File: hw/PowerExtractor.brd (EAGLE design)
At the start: 100 x 80 mm, 92 parts, among them IC1 LM358D, Q1 BSS84, Q3 BC847SMD, Q4 BC847SMD, Q5 BC847SMD, Q6 BC847SMD, T1 IRL530N, T2 IRF7416, T3 IRLL014N_, T4 IRLL014N_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

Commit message: Routing of board
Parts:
- moved JP9 59.3 mm to (50.8, 47.0)
- moved C7 51.0 mm to (59.7, 24.1)
- moved R5 50.6 mm to (59.7, 30.5)
- moved R18 35.0 mm to (57.1, 53.3), flipped to the bottom, turned to 0 degrees
- moved R4 34.3 mm to (57.1, 21.6), turned to 180 degrees
- moved R20 23.4 mm to (68.6, 31.8)
- moved OPH1 15.3 mm to (85.1, 63.5)
- moved D8 8.52 mm to (58.4, 62.2), turned to 180 degrees
- moved R7 7.73 mm to (48.3, 53.3), turned to 270 degrees
- moved D7 7.18 mm to (50.8, 55.9), turned to 270 degrees
- moved C8 5.08 mm to (50.8, 49.5)
- moved R9 4.02 mm to (55.9, 3.81), turned to 90 degrees
- moved R10 3.81 mm to (55.9, 11.4)
- moved Q4 3.59 mm to (55.9, 57.1)
- moved R17 3.59 mm to (59.7, 55.9)
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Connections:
- removed net N$21: HEAD_LED.1, U$1.VO+
- removed net N$22: HEAD_LED.2, U$1.VO-
- new net N$13: HEAD_LED.2, U$1.VO+
- new net N$15: HEAD_LED.1, U$1.VO-
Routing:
- net BAT+FUSED: track 23.3 -> 105.5 mm
- net GND: track 189.4 -> 266.8 mm
- net N$24: track 0.00 -> 57.8 mm
- net +5V: track 30.7 -> 73.0 mm
- net N$35: track 0.00 -> 41.4 mm
- net N$34: track 0.00 -> 40.4 mm
- net ARDUINO_VIN: track 0.00 -> 35.2 mm
- net N$19: track 0.00 -> 34.2 mm
- net ARDUINO_VOUT_SENSE: track 0.00 -> 31.5 mm
- net N$14: track 0.00 -> 23.8 mm
- net ARDUINO_LIGHT_IN: track 4.99 -> 26.7 mm
- net N$13: track 0.00 -> 15.5 mm
- net VIN: track 44.8 -> 53.4 mm
- net N$20: track 0.00 -> 8.51 mm
- net N$9: track 1.87 -> 9.69 mm
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
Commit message: Routing
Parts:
- IC1: value LM358D -> LM358N; device linear:SO08 -> linear:DIL08
- moved R12 10.2 mm to (74.9, 49.5), flipped to the top, turned to 180 degrees
- moved IC1 5.08 mm to (25.4, 57.1)
- moved R22 1.80 mm to (22.9, 55.9), flipped to the bottom, turned to 180 degrees
- moved R23 1.27 mm to (22.9, 58.4), flipped to the bottom, turned to 180 degrees
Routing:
- net N$24: track 57.8 -> 0.00 mm
- net ARDUINO_CHARGE_SENSE: track 1.27 -> 44.8 mm
- net +5V: track 73.0 -> 34.4 mm
- net GND: track 266.8 -> 300.9 mm
- net ARDUINO_ROTATION_INT: track 2.60 -> 25.8 mm
- net N$5: track 8.50 -> 0.00 mm
- net N$8: track 6.57 -> 2.84 mm
- net ARDUINO_LIGHT_IN: track 26.7 -> 29.4 mm
- net N$27: track 2.40 -> 0.00 mm
- net N$11: track 1.27 -> 2.54 mm

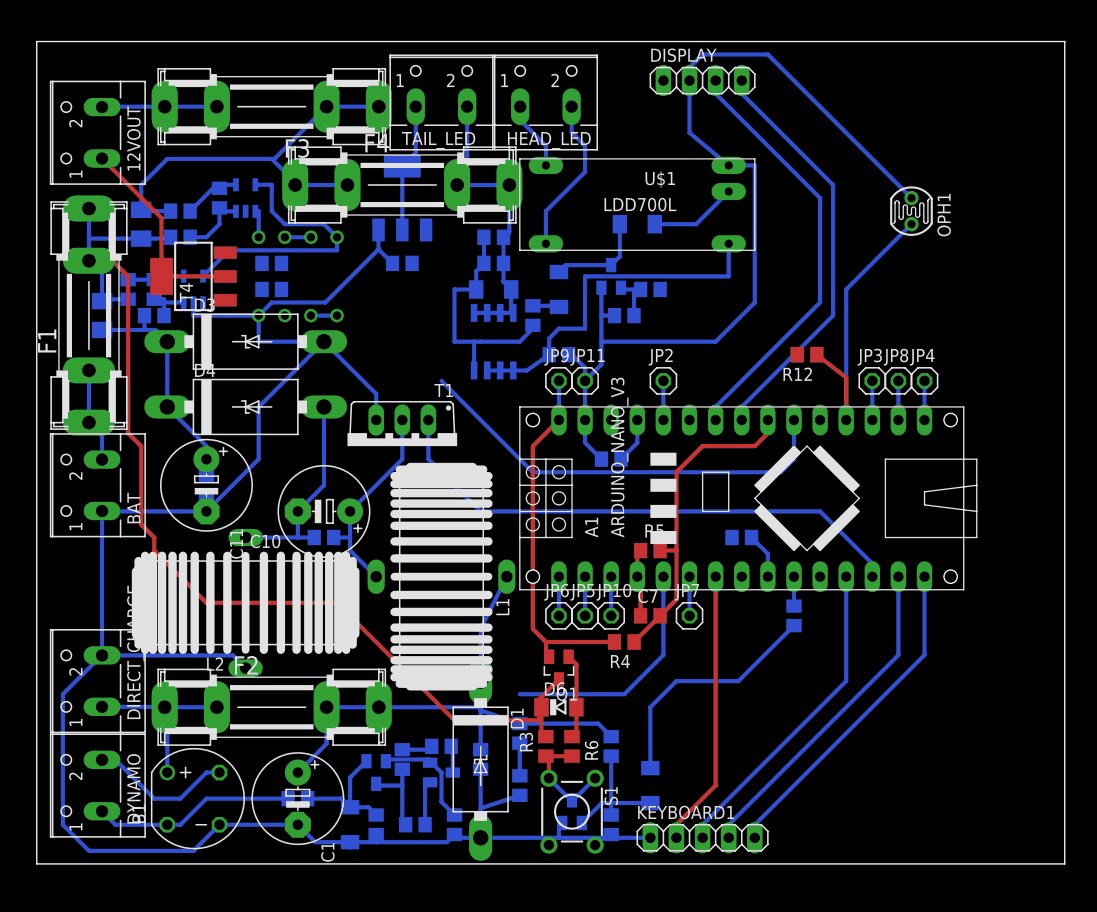
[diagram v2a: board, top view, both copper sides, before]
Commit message: Refactored layout
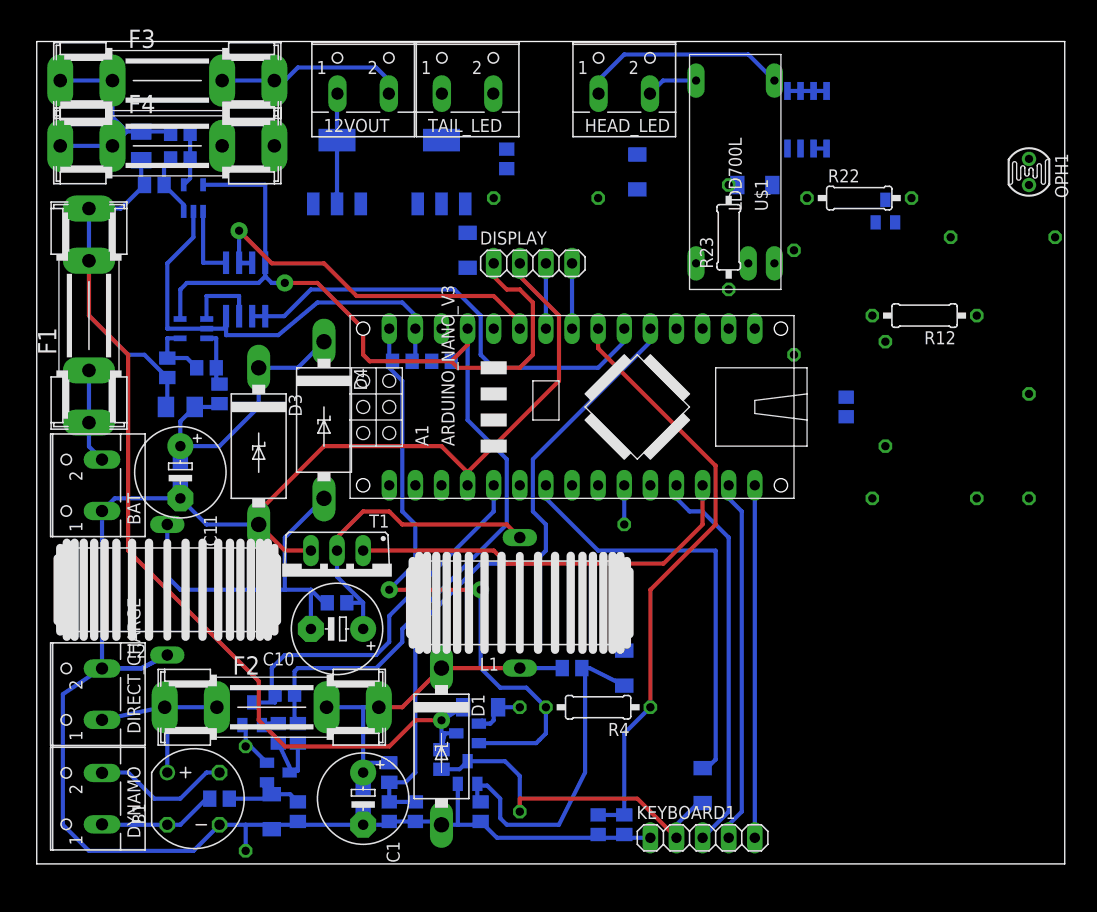
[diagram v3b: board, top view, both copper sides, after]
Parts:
- removed JP10, JP11, JP2, JP3, JP4, JP5, JP6, JP7, JP8, JP9: (no value), pinhead:1X01
- removed S1: (no value), triakcz:TL1105
- added C12: 10n, rcl:C0805
- added C14: 1uF/50V, rcl:C0805
- added D10: 1N4148MINIMELF, triakcz:SOD80C
- IC1: value LM358N -> LM358D; device linear:DIL08 -> linear:SO08
- R1, R10, R15, R16, R24, R25, R29, R3, R30, R31, R5, R9: device rcl:R0805 -> rcl:M0805
- R11, R12, R17, R18, R19, R20, R21, R22, R23, R26, R4, R6, R7: device rcl:R0805 -> rcl:0207/10
- moved R22 57.8 mm to (80.0, 64.8), flipped to the top, turned to 0 degrees
- moved R21 55.7 mm to (86.4, 35.6)
- moved R7 49.9 mm to (96.5, 40.6)
- moved R23 44.5 mm to (67.3, 61.0), flipped to the top, turned to 90 degrees
- moved R18 37.6 mm to (94.0, 61.0)
- moved T2 37.4 mm to (74.9, 72.4)
- moved C8 28.4 mm to (78.7, 44.5), turned to 270 degrees
- moved Q4 27.4 mm to (82.5, 63.5)
- moved 12VOUT 27.1 mm to (31.8, 76.2), turned to 0 degrees
- moved R5 26.8 mm to (57.1, 3.81), flipped to the bottom, turned to 90 degrees
- moved DISPLAY 24.3 mm to (48.3, 58.4)
- moved F4 23.2 mm to (12.7, 69.8)
- moved C7 20.9 mm to (54.6, 3.81), flipped to the bottom, turned to 90 degrees
- moved R26 20.5 mm to (20.3, 6.35)
- moved R20 19.8 mm to (82.5, 45.7), turned to 270 degrees
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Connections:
- removed net N$33: A1.D4, KEYBOARD1.2
- removed net N$38: A1.D1/TX, JP6.1
- removed net N$39: A1.D0/RX, JP5.1
- removed net N$40: A1.D3, JP7.1
- removed net N$42: A1.A7, JP2.1
- removed net N$43: A1.REF, JP3.1
- removed net N$44: A1.RST.1, A1.RST.2, JP10.1
- removed net N$45: A1.D13, JP4.1
- new net N$22: A1.D4, D10.C
- net +3V3: no longer JP8.1
- net ARDUINO_VIN: now also C14.1; no longer JP9.1
- net ARDUINO_VIN_ANALOG: now also C12.2
- net GND: now also C12.1, C14.2; no longer JP11.1, S1.1, S1.2
- net N$6: now also D10.A, KEYBOARD1.2; no longer S1.3, S1.4
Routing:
- net +5V: track 34.4 -> 130.6 mm, vias 0 -> 1
- net ARDUINO_VIN_ANALOG: track 3.18 -> 64.1 mm
- net GND: track 300.9 -> 240.1 mm
- net N$22: track 0.00 -> 41.8 mm
- net N$35: track 41.4 -> 6.35 mm
- net N$11: track 2.54 -> 37.4 mm, vias 0 -> 1
- net N$34: track 40.4 -> 6.35 mm
- net N$19: track 34.2 -> 1.27 mm
- net ARDUINO_LIGHT_IN: track 29.4 -> 0.00 mm
- net N$33: track 27.0 -> 0.00 mm
- net ARDUINO_VOUT_SENSE: track 31.5 -> 58.3 mm
- net ARDUINO_VIN: track 35.2 -> 61.8 mm, vias 0 -> 2
- net LIGHTVCC: track 30.0 -> 3.81 mm
- net N$6: track 11.1 -> 35.3 mm
- net N$14: track 23.8 -> 0.00 mm
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
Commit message: Completely routed
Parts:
- removed OPH1: VT90N1, photo-elements:VT900
- removed T3, T4: IRLL014N_, triakcz:SOT223
- added PHOTORESIST: (no value), pinhead:1X02
- added Q2: IRL530, transistor-power:TO220BV
- added Q7: IRF530, transistor-power:TO220BV
- R18, R19, R21, R7: device rcl:0207/10 -> rcl:M0805
- R23: device rcl:0207/10 -> rcl:R0805
- moved R21 63.1 mm to (30.5, 64.8), flipped to the top, turned to 90 degrees
- moved R7 52.2 mm to (52.1, 67.9), turned to 0 degrees
- moved R23 44.5 mm to (22.9, 63.5)
- moved R20 37.5 mm to (48.3, 61.0), turned to 180 degrees
- moved C8 33.7 mm to (55.2, 68.6), flipped to the top, turned to 90 degrees
- moved R12 33.1 mm to (53.3, 55.9)
- moved R22 32.4 mm to (48.3, 58.4)
- moved T2 32.0 mm to (43.2, 68.6), turned to 270 degrees
- moved R18 24.8 mm to (69.2, 59.7), turned to 270 degrees
- moved D7 16.5 mm to (57.1, 66.0), turned to 0 degrees
- moved Q4 15.2 mm to (67.3, 63.5)
- moved R17 14.4 mm to (63.5, 44.5), turned to 0 degrees
- moved D10 8.25 mm to (61.6, 15.2)
- moved R19 7.41 mm to (53.3, 71.1), turned to 90 degrees
- moved D8 6.54 mm to (64.1, 62.9), turned to 270 degrees
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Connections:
- net ARDUINO_LIGHT_IN: now also PHOTORESIST.2; no longer OPH1.1
- net GND: now also PHOTORESIST.1, Q2.S, Q7.S; no longer OPH1.2, T3.3, T4.3
- net N$24: now also Q2.G; no longer T3.1
- net N$25: now also Q2.D; no longer T3.2, T3.4
- net N$27: now also Q7.G; no longer T4.1
- net N$28: now also Q7.D; no longer T4.2, T4.4
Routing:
- net GND: track 240.1 -> 371.2 mm
- net LIGHTVCC: track 3.81 -> 55.9 mm
- net N$19: track 1.27 -> 46.3 mm, vias 0 -> 1
- net ARDUINO_LIGHT_IN: track 0.00 -> 41.3 mm
- net ARDUINO_OUT_TAIL_LIGHT: track 0.00 -> 31.5 mm
- net ARDUINO_OUT_CHARGE_OUTPUT_CONTROL: track 0.00 -> 24.2 mm
- net N$17: track 0.00 -> 22.0 mm
- net N$27: track 0.00 -> 22.0 mm
- net N$22: track 41.8 -> 24.9 mm
- net N$14: track 0.00 -> 14.9 mm
- net N$24: track 0.00 -> 14.8 mm
- net N$25: track 0.00 -> 14.2 mm
- net ARDUINO_MAIN_LIGHT_CTRL: track 0.00 -> 10.3 mm
- net N$9: track 0.00 -> 9.09 mm
- net N$26: track 38.2 -> 31.5 mm
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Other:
- board size 100 x 80 mm -> 74.6 x 80 mm

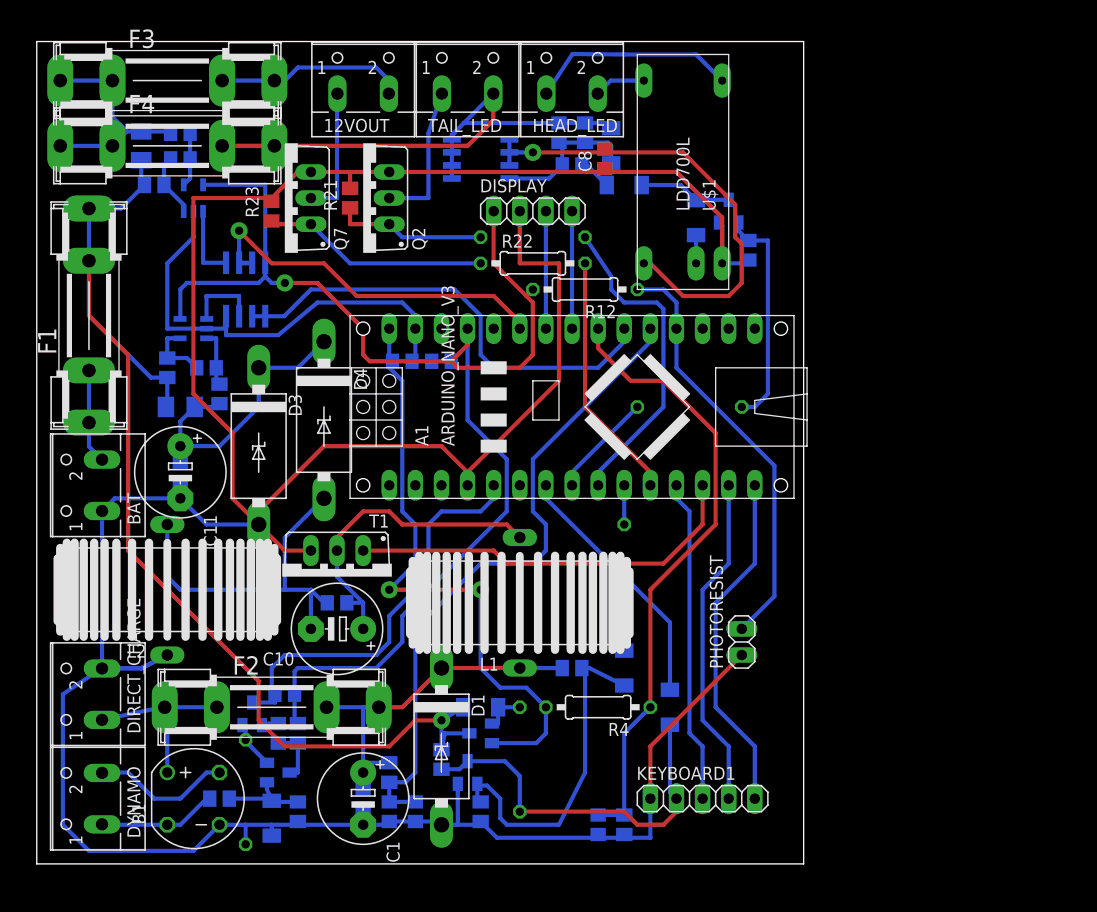
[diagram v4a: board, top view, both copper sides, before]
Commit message: set reasonable width of power lines
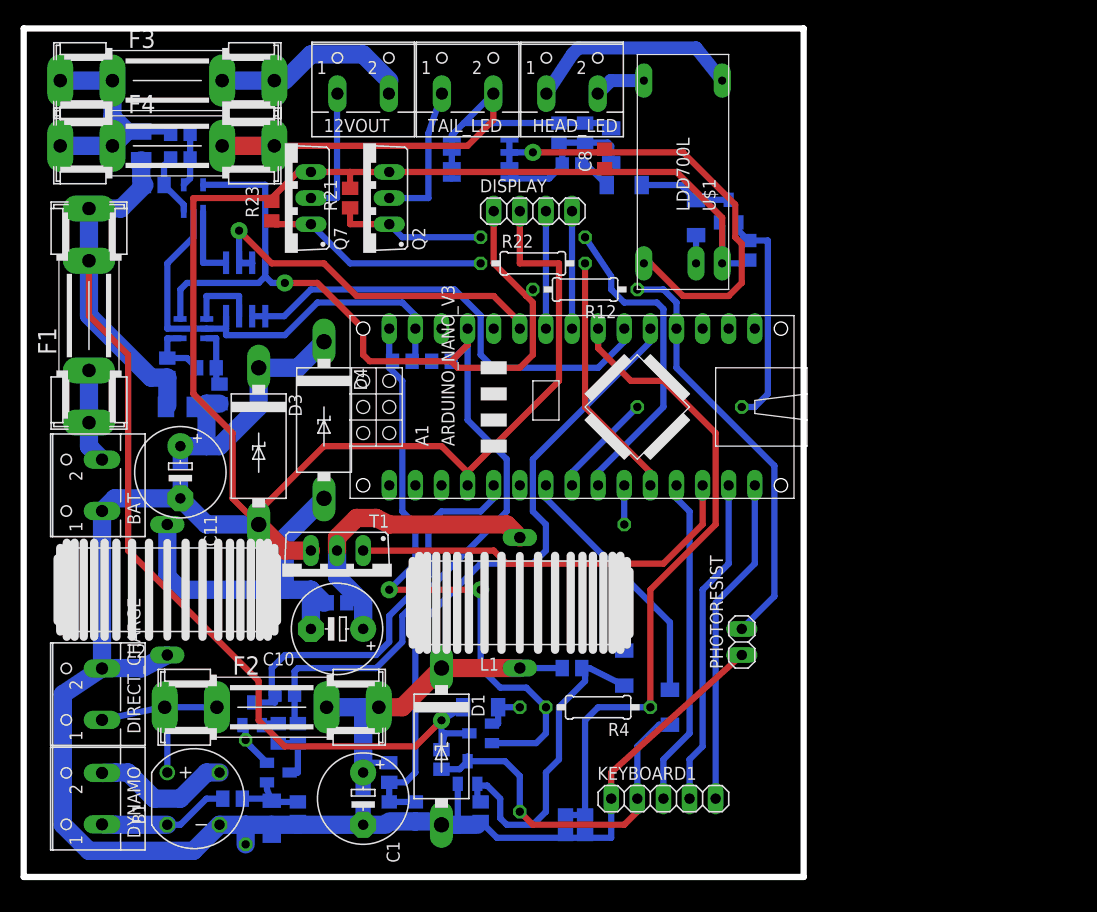
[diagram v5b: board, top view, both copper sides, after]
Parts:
- moved KEYBOARD1 3.81 mm to (61.0, 6.35)
- moved R5 3.81 mm to (53.3, 3.81)
- moved C7 3.17 mm to (51.4, 3.81)
- moved R24 1.27 mm to (19.1, 6.35)
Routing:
- net ARDUINO_VOUT_SENSE: track 60.1 -> 64.0 mm
- net N$6: track 37.5 -> 35.4 mm
- net N$36: track 33.6 -> 32.1 mm
- net GND: track 371.2 -> 369.9 mm
- net HUB_1: track 11.5 -> 12.8 mm
- net N$29: track 8.65 -> 7.38 mm
- net +OUT: track 18.6 -> 19.6 mm
- net N$4: track 33.0 -> 31.9 mm
- net OUTPUT_TO_SENSE: track 28.9 -> 29.9 mm
- net N$15: track 20.2 -> 20.9 mm
- net N$2: track 31.4 -> 30.8 mm
- net N$37: track 32.6 -> 32.1 mm
- net N$26: track 31.5 -> 32.1 mm
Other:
- board size 74.6 x 80 mm -> 75.9 x 82.5 mm

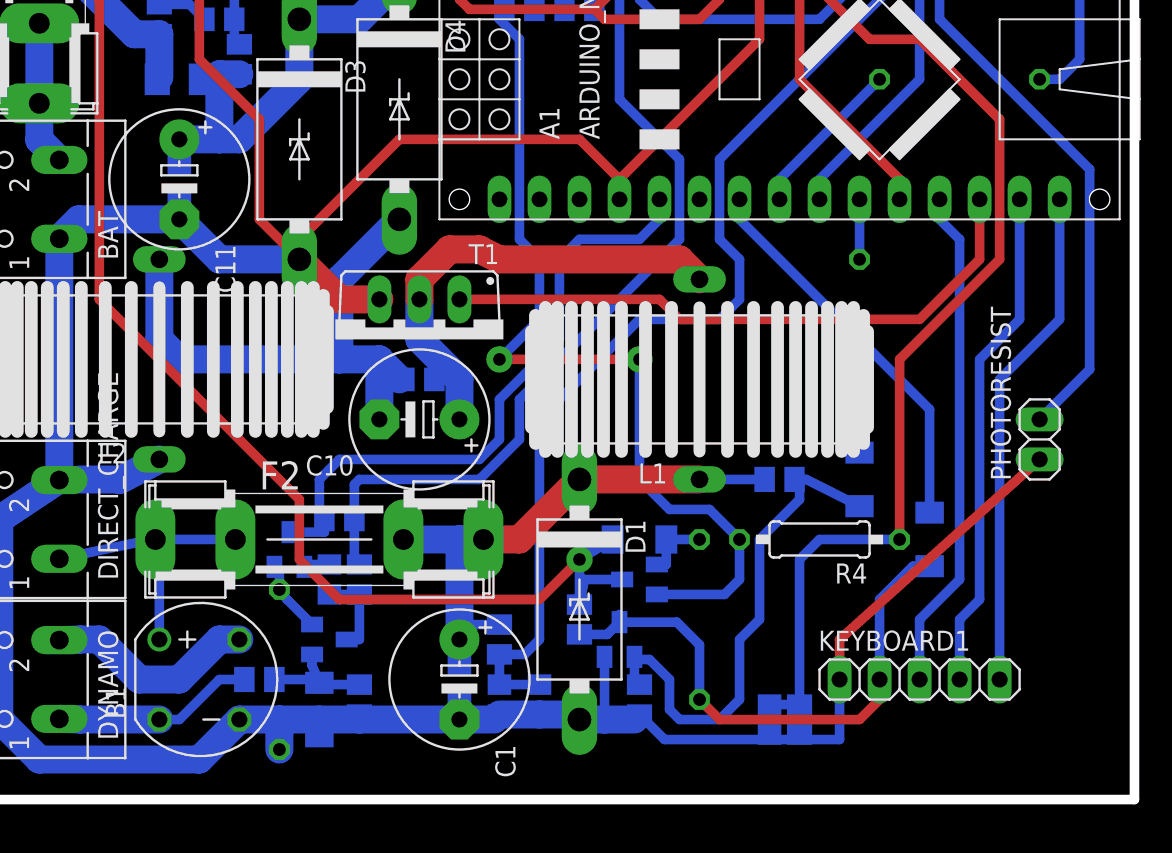
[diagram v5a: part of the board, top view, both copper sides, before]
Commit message: Fixed speed sense circuit
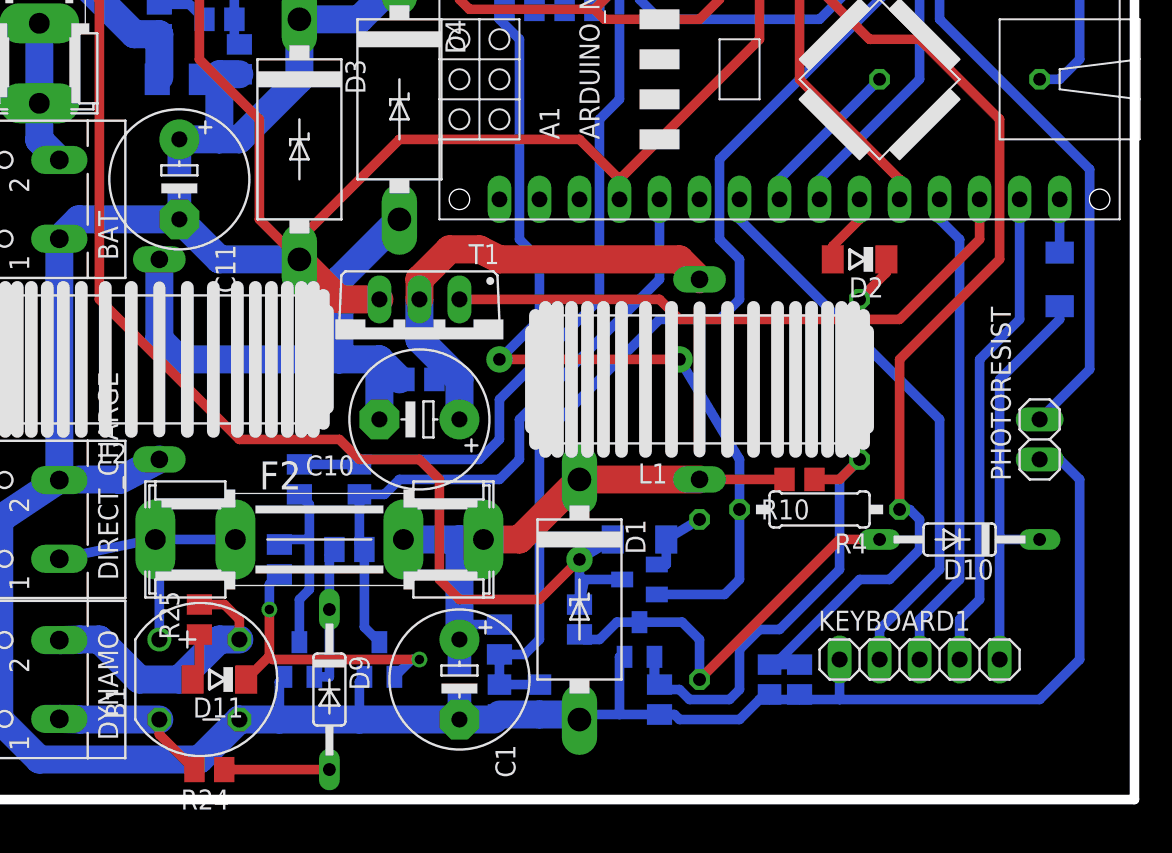
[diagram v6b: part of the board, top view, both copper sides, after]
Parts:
- removed Q3, Q5, Q6: BC847SMD, triakcz:SOT23
- removed R27: 470R, rcl:R0805
- added D11, D12: 1N4148MINIMELF, triakcz:SOD80C
- added R8: 100k, rcl:M0805
- added U$2, U$3, U$4: BCV47, triakcz:SOT23
- D10, D9: value 1N4148MINIMELF -> 1N4148DO35-10; device triakcz:SOD80C -> triakcz:DO35-10
- R10: device rcl:M0805 -> rcl:R0805
- R25: value 330k -> 330K
- R26: value 470R -> 100k; device rcl:0207/10 -> rcl:M0805
- moved D2 14.0 mm to (57.1, 33.0), flipped to the top, turned to 180 degrees
- moved R25 11.4 mm to (15.2, 10.2), flipped to the top
- moved R26 8.82 mm to (24.8, 14.6), turned to 0 degrees
- moved R29 7.41 mm to (21.6, 19.1)
- moved R24 6.54 mm to (15.9, 0.64), flipped to the top, turned to 180 degrees
- moved R28 2.84 mm to (25.4, 19.1), turned to 90 degrees
- moved R11 2.54 mm to (57.1, 25.4)
- moved C7 2.54 mm to (51.4, 6.35)
- moved R5 2.54 mm to (53.3, 6.35)
- moved D10 1.91 mm to (63.5, 15.2), flipped to the top, turned to 180 degrees
- moved R4 1.90 mm to (54.6, 17.1)
- moved D9 1.42 mm to (23.5, 5.71), flipped to the top
- moved R10 1.27 mm to (53.3, 19.1), flipped to the top, turned to 180 degrees
- moved R9 1.27 mm to (44.5, 5.08)
- moved KEYBOARD1 1.27 mm to (61.0, 7.62)
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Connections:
- new net N$38: D11.A, R25.1
- new net N$39: A1.D12, D12.A
- net ARDUINO_ROTATION_INT: now also R26.1, U$2.3; no longer Q6.3
- net ARDUINO_SELF_POWER_OUT: now also D2.A; no longer R11.2
- net GND: now also U$2.2, U$3.2, U$4.2; no longer D9.A, Q3.2, R25.1, R26.1
- net HUB2: now also R25.2
- net N$12: now also D2.C, R11.2; no longer D2.A, R11.1
- net N$22: now also D10.A, R3.1, R6.2, U$4.3; no longer A1.D4, D10.C
- net N$29: now also D9.A; no longer D9.C, Q5.1, R25.2
- net N$30: now also R8.2, U$3.3; no longer Q5.3, R27.1
- net N$31: now also D9.C, U$3.1; no longer Q5.2, Q6.2
- net N$32: now also D11.C, R8.1, U$2.1; no longer Q6.1, R27.2
- net N$36: now also D10.C, D12.C; no longer A1.D12
- net N$4: now also R11.1, U$4.1; no longer D2.C, Q3.1
- net N$6: now also A1.D4; no longer D10.A, Q3.3, R3.1, R6.2
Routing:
- net N$32: track 1.73 -> 19.2 mm, vias 0 -> 2
- net GND: track 369.9 -> 383.1 mm
- net N$30: track 5.57 -> 11.9 mm
- net +5V: track 135.8 -> 129.5 mm
- net N$36: track 32.1 -> 26.5 mm
- net N$31: track 4.62 -> 9.17 mm
- net HUB2: track 13.5 -> 17.7 mm
- net N$39: track 0.00 -> 3.38 mm
- net N$38: track 0.00 -> 3.04 mm
- net HUB_1: track 12.8 -> 10.4 mm
- net BAT+FUSED: track 115.8 -> 117.3 mm
- net ARDUINO_VOUT_SENSE: track 64.0 -> 62.6 mm
- net N$22: track 24.9 -> 26.3 mm
- net VIN: track 35.9 -> 37.2 mm
- net N$37: track 32.1 -> 30.8 mm
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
